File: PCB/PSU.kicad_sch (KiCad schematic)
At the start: 38 parts, among them U1 AP2127K-3.3, U7 AP2127K-ADJ

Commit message: More routing
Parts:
- removed C24, C5: 1u, Capacitor_SMD:C_0603_1608Metric, symbol Device:C_Small
- removed R16: 10k, Resistor_SMD:R_0402_1005Metric, symbol Device:R_Small
- removed R18: 15k, Resistor_SMD:R_0402_1005Metric, symbol Device:R_Small
- removed U7: AP2127K-ADJ, Package_TO_SOT_SMD:SOT-23-5, symbol Regulator_Linear:AP2127K-ADJ

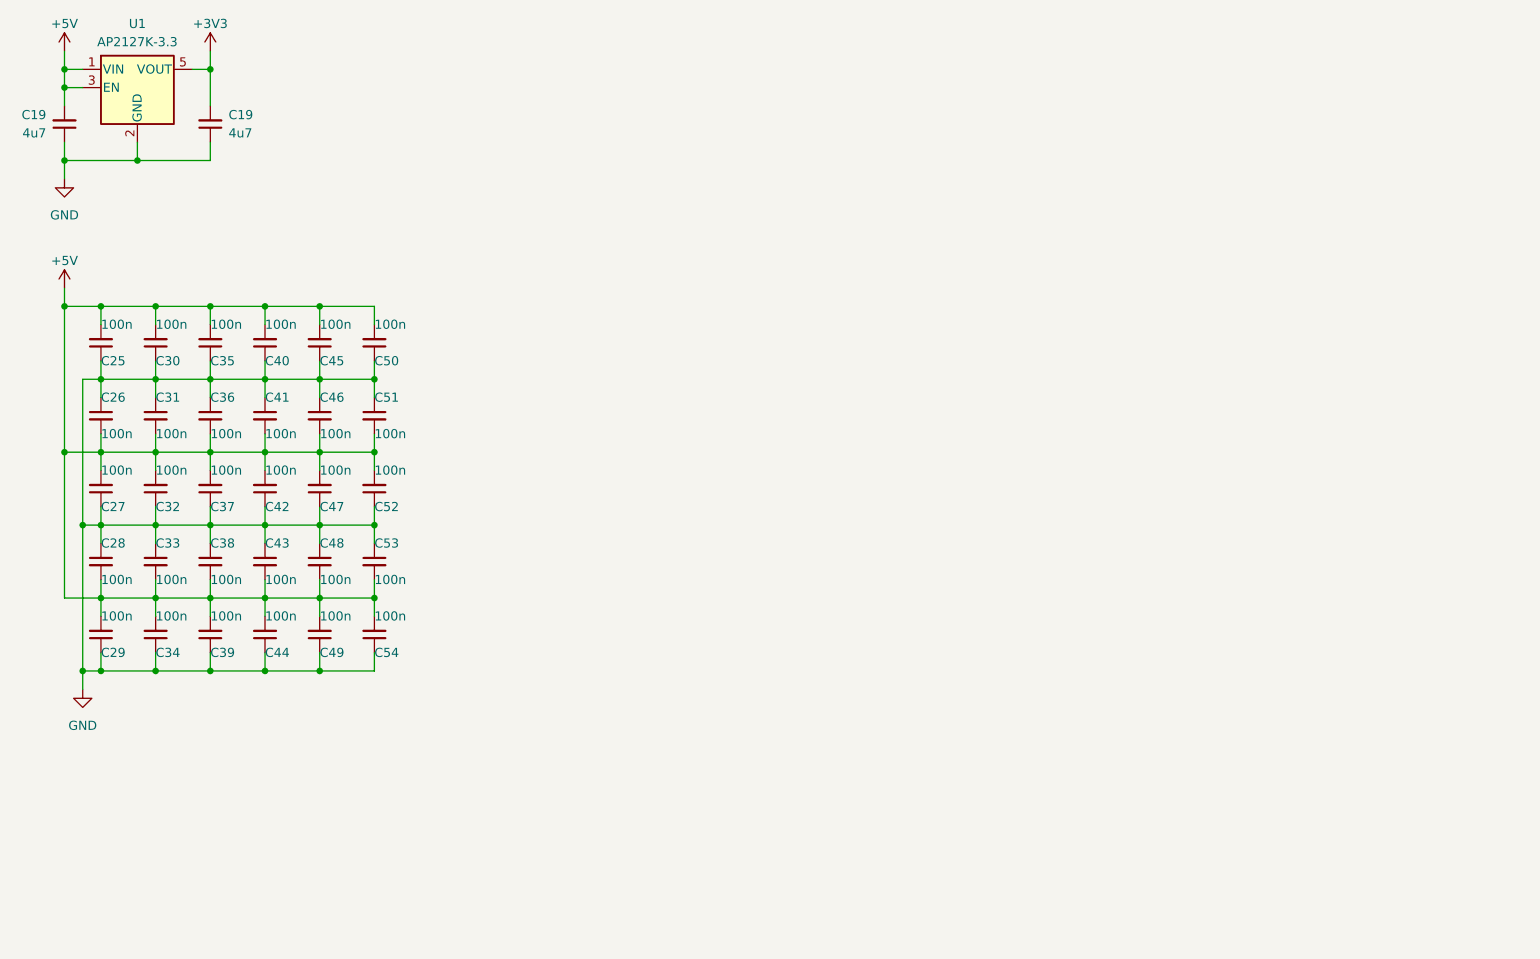
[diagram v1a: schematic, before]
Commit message: 08/08/2023 update
Removed Ogen footprint, and future VIK support is planned. Rerouted board following latest Honeydew revision. WIP support for the USB2541 is added, but it's very tentative and not yet complete. Added CX70M-24P1 footprint.
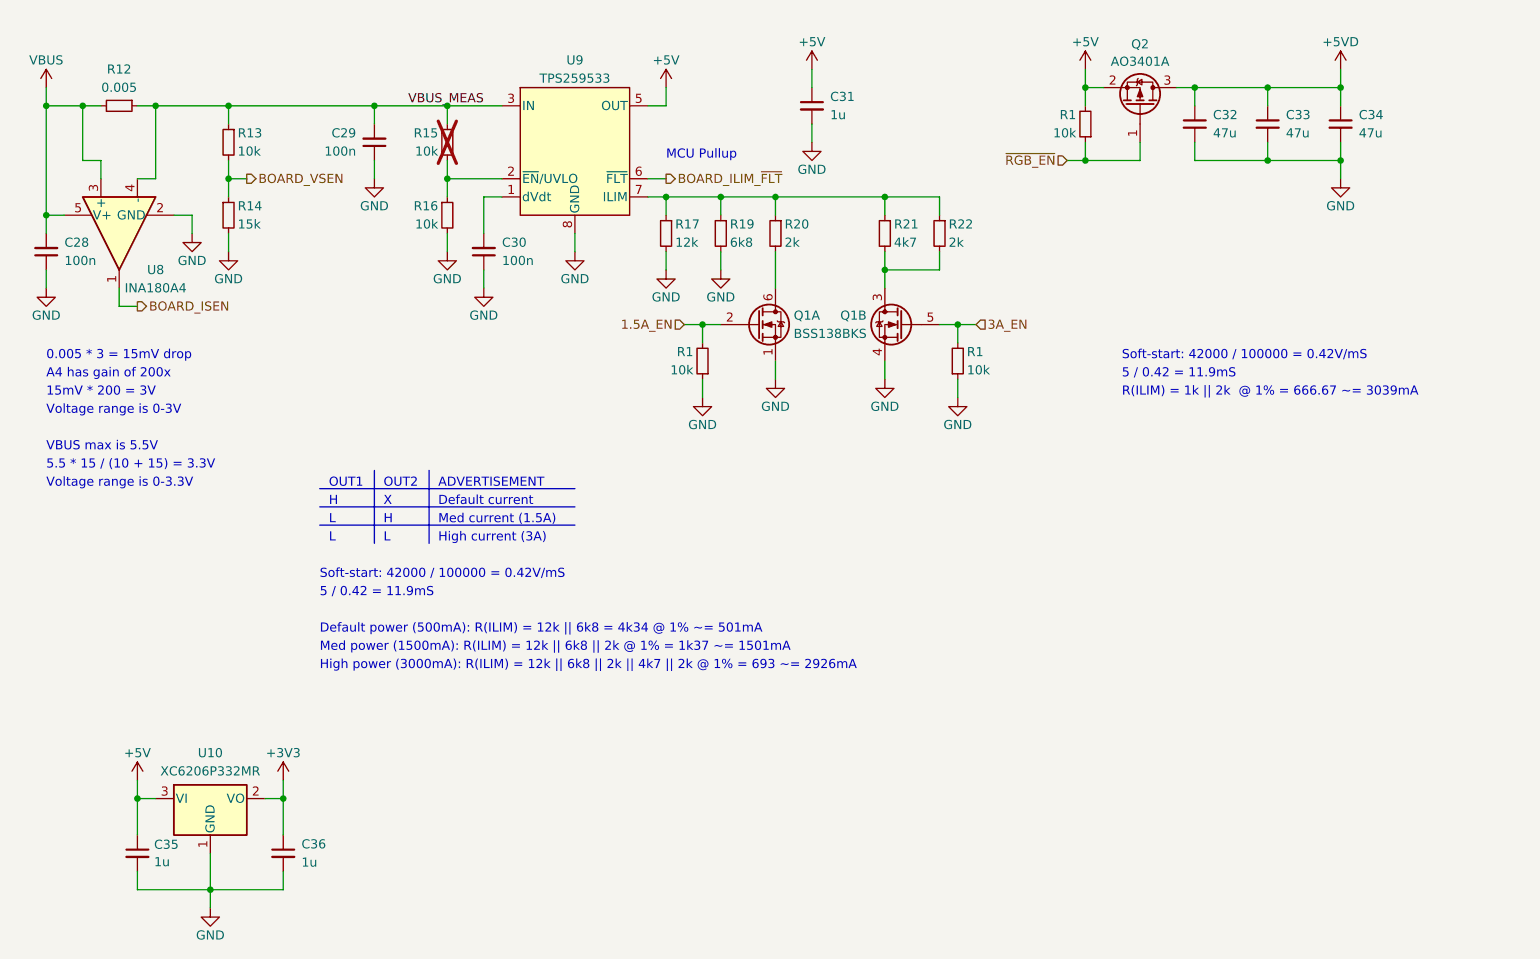
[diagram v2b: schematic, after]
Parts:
- removed C19 (x2): 4u7, Capacitor_SMD:C_0603_1608Metric, symbol Device:C_Small
- removed C25, C26, C27, C37, C38, C39, C40, C41, C42, C43, C44, C45, C46, C47, C48, C49, C50, C51, C52, C53, C54: 100n, Cantaloupe:C_0402_1005Metric, symbol Device:C_Small
- removed U1: AP2127K-3.3, Package_TO_SOT_SMD:SOT-23-5, symbol Regulator_Linear:AP2127K-3.3
- added Q1: BSS138BKS, Cantaloupe:SOT-363_SC-70-6, symbol Device:Q_Dual_NMOS_S1G1D2S2G2D1
- added Q2: AO3401A, Cantaloupe:SOT-23-3, symbol Transistor_FET:AO3401A
- added R1 (x3), R13, R15, R16: 10k, Resistor_SMD:R_0402_1005Metric, symbol Device:R_Small
- added R12: 0.005, Resistor_SMD:R_0805_2012Metric, symbol Device:R_Small
- added R14: 15k, Resistor_SMD:R_0402_1005Metric, symbol Device:R_Small
- added R17: 12k, Resistor_SMD:R_0402_1005Metric, symbol Device:R_Small
- added R19: 6k8, Resistor_SMD:R_0402_1005Metric, symbol Device:R_Small
- added R20, R22: 2k, Resistor_SMD:R_0402_1005Metric, symbol Device:R_Small
- added R21: 4k7, Resistor_SMD:R_0402_1005Metric, symbol Device:R_Small
- added U10: XC6206P332MR, Cantaloupe:SOT-23-3, symbol Regulator_Linear:XC6206PxxxMR
- added U8: INA180A4, Package_TO_SOT_SMD:SOT-23-5, symbol Amplifier_Current:INA180A4
- added U9: TPS259533, Cantaloupe:WSON-8-1EP_2x2mm_P0.5mm_EP0.9x1.6mm, symbol Honeydew:TPS259533
- C28, C29, C30: footprint Cantaloupe:C_0402_1005Metric -> Capacitor_SMD:C_0402_1005Metric; LCSC C1525 -> C307331; Voltage (none) -> 50V
- C31, C35, C36: value 100n -> 1u; footprint Cantaloupe:C_0402_1005Metric -> Capacitor_SMD:C_0402_1005Metric; LCSC C1525 -> C52923; Voltage (none) -> 25V
- C32, C33, C34: value 100n -> 47u; footprint Cantaloupe:C_0402_1005Metric -> Capacitor_SMD:C_1206_3216Metric; LCSC C1525 -> C96123; Voltage (none) -> 10V
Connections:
- net +3V3: now also C36.1, U10.2 (VO)
- net +5V: now also C31.1, C35.1, Q2.2 (S), R1.2, U10.3 (VI), U9.5 (OUT); no longer C28.2, C29.2, C30.2, C31.2, C32.2, C33.2, C34.2, C35.2, C36.2
- net GND: now also C31.2, C32.2, C33.2, C34.2, C35.2, C36.2, Q1.1 (S), Q1.4 (S), R1.1, R1.1, R14.2, R16.2, R17.2, R19.2, U10.1 (GND), U8.2 (GND), U9.8 (GND), U9.9 (GND); no longer C31.1, C32.1, C33.1, C34.1, C35.1, C36.1
- new net: Q1.3 (D), R21.2, R22.2
- new net: C30.2, U9.1 (dVdt)
- new net: R15.1, R16.1, U9.2 (~{EN}/UVLO)
- new net: R17.1, R19.1, R20.1, R21.1, R22.1, U9.7 (ILIM)
- new net: Q1.6 (D), R20.2
- new net +5VD: C32.1, C33.1, C34.1, Q2.3 (D)
- new net 1.5A_EN: Q1.2 (G), R1.2
- new net 3A_EN: Q1.5 (G), R1.2
- new net BOARD_ILIM_~{FLT}: U9.6 (~{FLT})
- new net BOARD_ISEN: U8.1
- new net BOARD_VSEN: R13.2, R14.1
- new net VBUS: C28.2, R12.2, U8.3 (+), U8.5 (V+)
- new net VBUS_MEAS: C29.2, R12.1, R13.1, R15.2, U8.4 (-), U9.3 (IN), U9.4 (IN)
- new net ~{RGB_EN}: Q2.1 (G), R1.1
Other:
- note added: "0.005 * 3 = 15mV drop"
- note added: "15mV * 200 = 3V"
- note added: "5 / 0.42 = 11.9mS"
- note added: "5.5 * 15 / (10 + 15) = 3.3V"
- note added: "A4 has gain of 200x"
- note added: "ADVERTISEMENT"
- note added: "Default current"
- note added: "Default power (500mA): R(ILIM) = 12k || 6k8 = 4k34 @ 1% ~= 501mA"
- note added: "H"
- note added: "High current (3A)"
- note added: "High power (3000mA): R(ILIM) = 12k || 6k8 || 2k || 4k7 || 2k @ 1% = 693 ~= 2926mA"
- note added: "L"
- note added: "MCU Pullup"
- note added: "Med current (1.5A)"
- note added: "Med power (1500mA): R(ILIM) = 12k || 6k8 || 2k @ 1% = 1k37 ~= 1501mA"
- note added: "OUT1"
- note added: "OUT2"
- note added: "R(ILIM) = 1k || 2k @ 1% = 666.67 ~= 3039mA"
- note added: "Soft-start: 42000 / 100000 = 0.42V/mS"
- note added: "VBUS max is 5.5V"
- note added: "Voltage range is 0-3.3V"
- note added: "Voltage range is 0-3V"
- note added: "X"
- company: (none) -> Created by Ariamelon (https://github.com/Ariamelon/Cantaloupe/)
- title: (none) -> Cantaloupe split ergonomic keyboard

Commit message: 23/08/2023 update
Changed MCU to nRF52840. Added nPM1300 PMIC for power management. Replaced SSD1351 display with Nice!View. Added Kailh Choc V1/V2 and Gateron KS-27/KS-33 support.
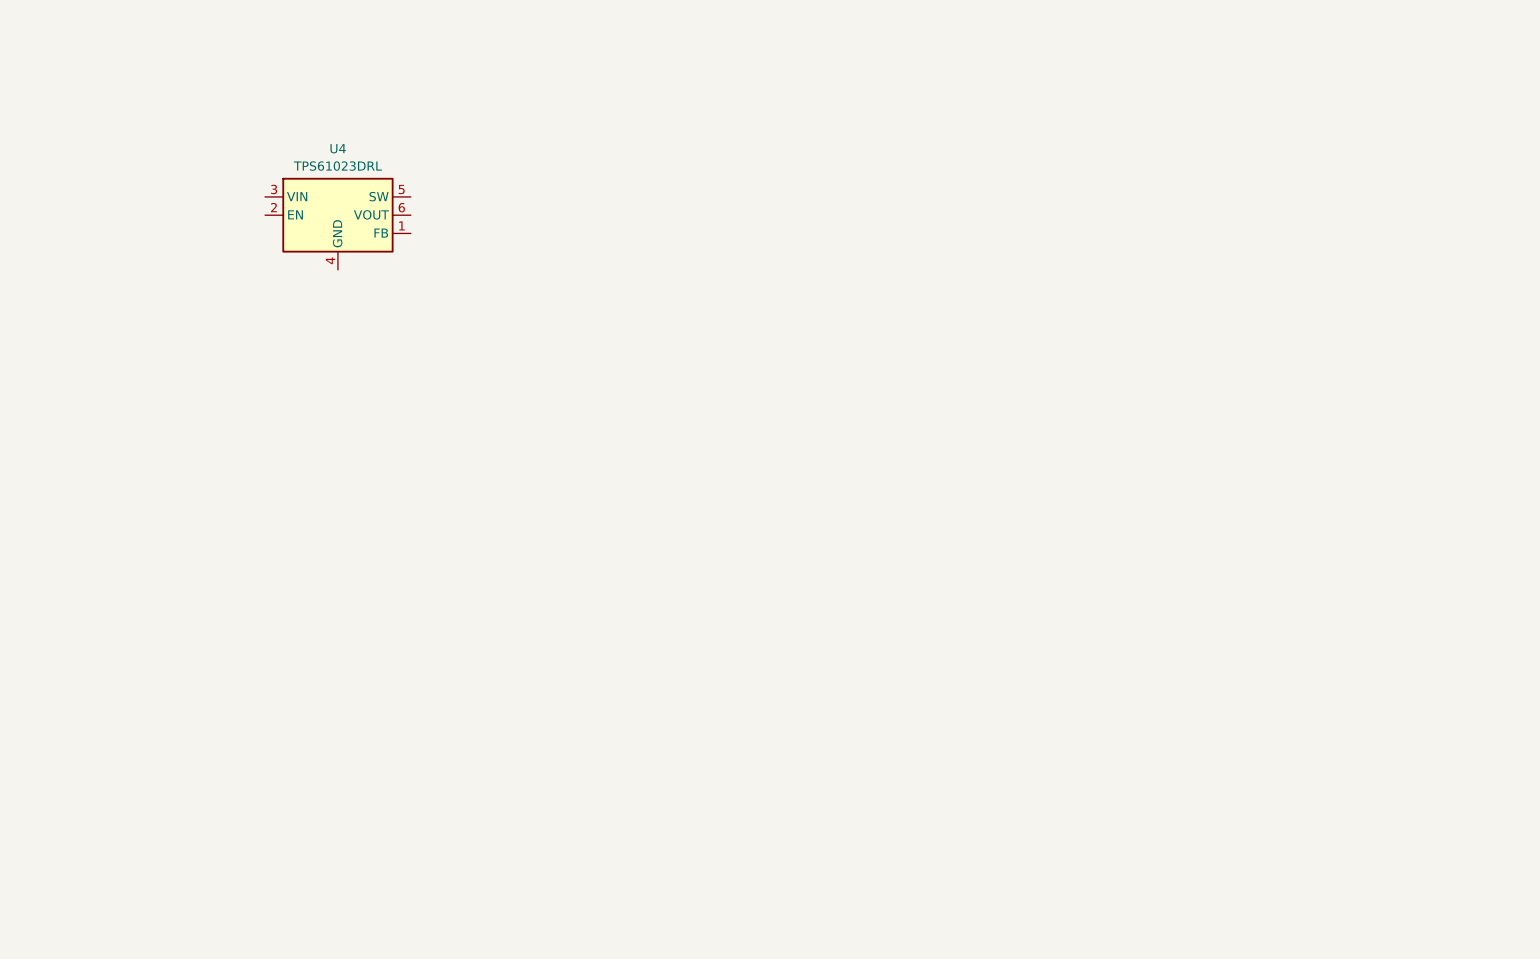
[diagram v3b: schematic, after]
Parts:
- removed C28, C29, C30: 100n, Capacitor_SMD:C_0402_1005Metric, symbol Device:C_Small
- removed C31, C35, C36: 1u, Capacitor_SMD:C_0402_1005Metric, symbol Device:C_Small
- removed C32, C33, C34: 47u, Capacitor_SMD:C_1206_3216Metric, symbol Device:C_Small
- removed Q1: BSS138BKS, Cantaloupe:SOT-363_SC-70-6, symbol Device:Q_Dual_NMOS_S1G1D2S2G2D1
- removed Q2: AO3401A, Cantaloupe:SOT-23-3, symbol Transistor_FET:AO3401A
- removed R1 (x3), R13, R15, R16: 10k, Resistor_SMD:R_0402_1005Metric, symbol Device:R_Small
- removed R12: 0.005, Resistor_SMD:R_0805_2012Metric, symbol Device:R_Small
- removed R14: 15k, Resistor_SMD:R_0402_1005Metric, symbol Device:R_Small
- removed R17: 12k, Resistor_SMD:R_0402_1005Metric, symbol Device:R_Small
- removed R19: 6k8, Resistor_SMD:R_0402_1005Metric, symbol Device:R_Small
- removed R20, R22: 2k, Resistor_SMD:R_0402_1005Metric, symbol Device:R_Small
- removed R21: 4k7, Resistor_SMD:R_0402_1005Metric, symbol Device:R_Small
- removed U10: XC6206P332MR, Cantaloupe:SOT-23-3, symbol Regulator_Linear:XC6206PxxxMR
- removed U8: INA180A4, Package_TO_SOT_SMD:SOT-23-5, symbol Amplifier_Current:INA180A4
- removed U9: TPS259533, Cantaloupe:WSON-8-1EP_2x2mm_P0.5mm_EP0.9x1.6mm, symbol Honeydew:TPS259533
- added U4: TPS61023DRL, Package_TO_SOT_SMD:SOT-563, symbol Cantaloupe:TPS61023DRL
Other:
- note removed: "0.005 * 3 = 15mV drop"
- note removed: "15mV * 200 = 3V"
- note removed: "5 / 0.42 = 11.9mS"
- note removed: "5.5 * 15 / (10 + 15) = 3.3V"
- note removed: "A4 has gain of 200x"
- note removed: "ADVERTISEMENT"
- note removed: "Default current"
- note removed: "Default power (500mA): R(ILIM) = 12k || 6k8 = 4k34 @ 1% ~= 501mA"
- note removed: "H"
- note removed: "High current (3A)"
- note removed: "High power (3000mA): R(ILIM) = 12k || 6k8 || 2k || 4k7 || 2k @ 1% = 693 ~= 2926mA"
- note removed: "L"
- note removed: "MCU Pullup"
- note removed: "Med current (1.5A)"
- note removed: "Med power (1500mA): R(ILIM) = 12k || 6k8 || 2k @ 1% = 1k37 ~= 1501mA"
- note removed: "OUT1"
- note removed: "OUT2"
- note removed: "R(ILIM) = 1k || 2k @ 1% = 666.67 ~= 3039mA"
- note removed: "Soft-start: 42000 / 100000 = 0.42V/mS"
- note removed: "VBUS max is 5.5V"
- note removed: "Voltage range is 0-3.3V"
- note removed: "Voltage range is 0-3V"
- note removed: "X"
- company: Created by Ariamelon (https://github.com/Ariamelon/Cantaloupe/) -> (none)
- title: Cantaloupe split ergonomic keyboard -> (none)
